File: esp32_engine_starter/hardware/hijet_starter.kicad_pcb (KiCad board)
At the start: 2 copper layers, 98 x 90 mm, 56 parts, among them J1 12V IN, J2 OUT, J3 IN, J4 I2C, J5 ESP32 VIN row, J6 ESP32 3V3 row, J7 OBD-II CAN, J8 GPS, Q1 2SC1815, U1 M78AR05-1, U2 PC817, U3 PC817, U4 PC817, U5 PC817, U6 PC817, U7 PC817, U8 PC817, U9 MCP2562-E/P

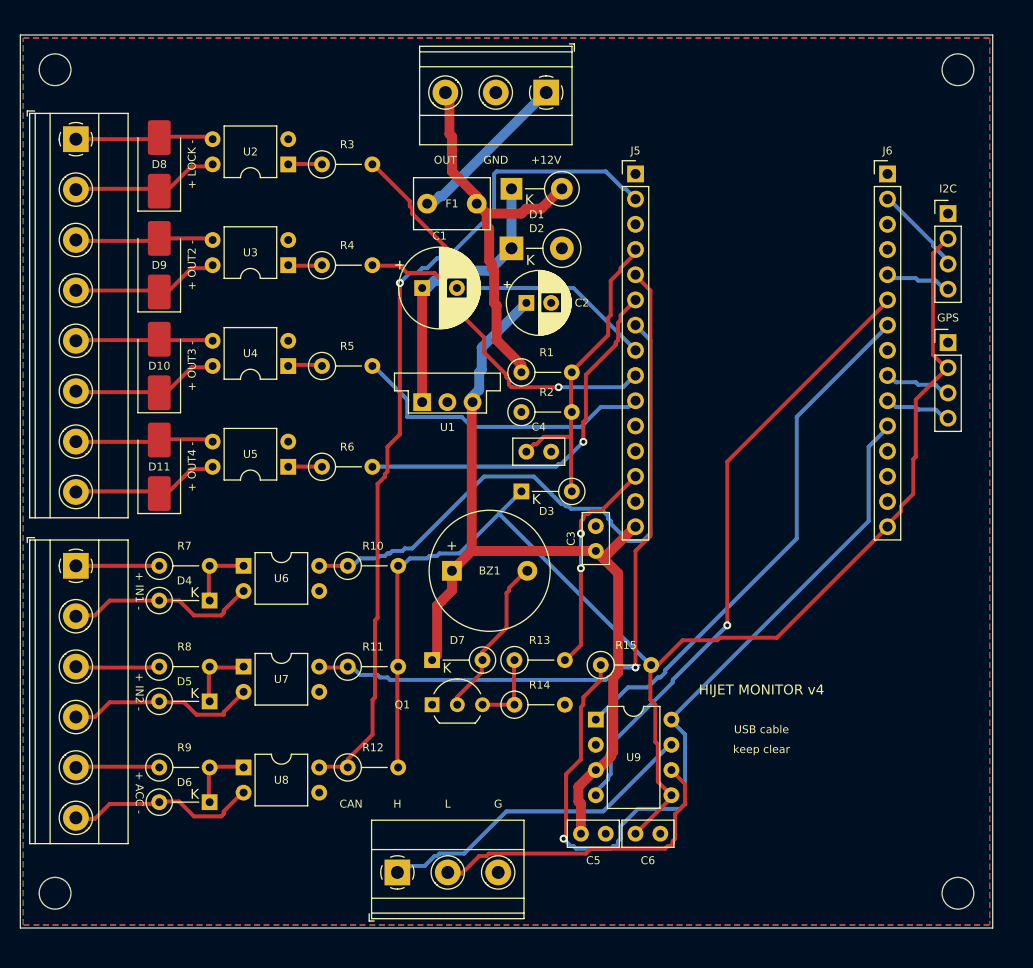
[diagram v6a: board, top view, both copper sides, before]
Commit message: ポリスイッチを RXEF110 に変更、逆接保護を SB340LS（3A）に変更
- RXEF090 が売り切れのため RXEF110（1.1A・72V）に変更
- RXEF の本体は幅 11〜13mm あり旧外形（7.5mm）では小さすぎたので、
  専用の外形（幅 12.8mm・穴 1.1mm）を作って基板上端に移動
- トリップまでの最大 2.2A に耐えるよう D1 を 1N5819（1A）から SB340LS（3A）へ
- 部品表・検証・文書を更新。全検証合格

Co-Authored-By: Claude Opus 5.5 <noreply@anthropic.com>
Claude-Session: https://claude.ai/code/session_011cXkDUypHbxixpJEznYmeT
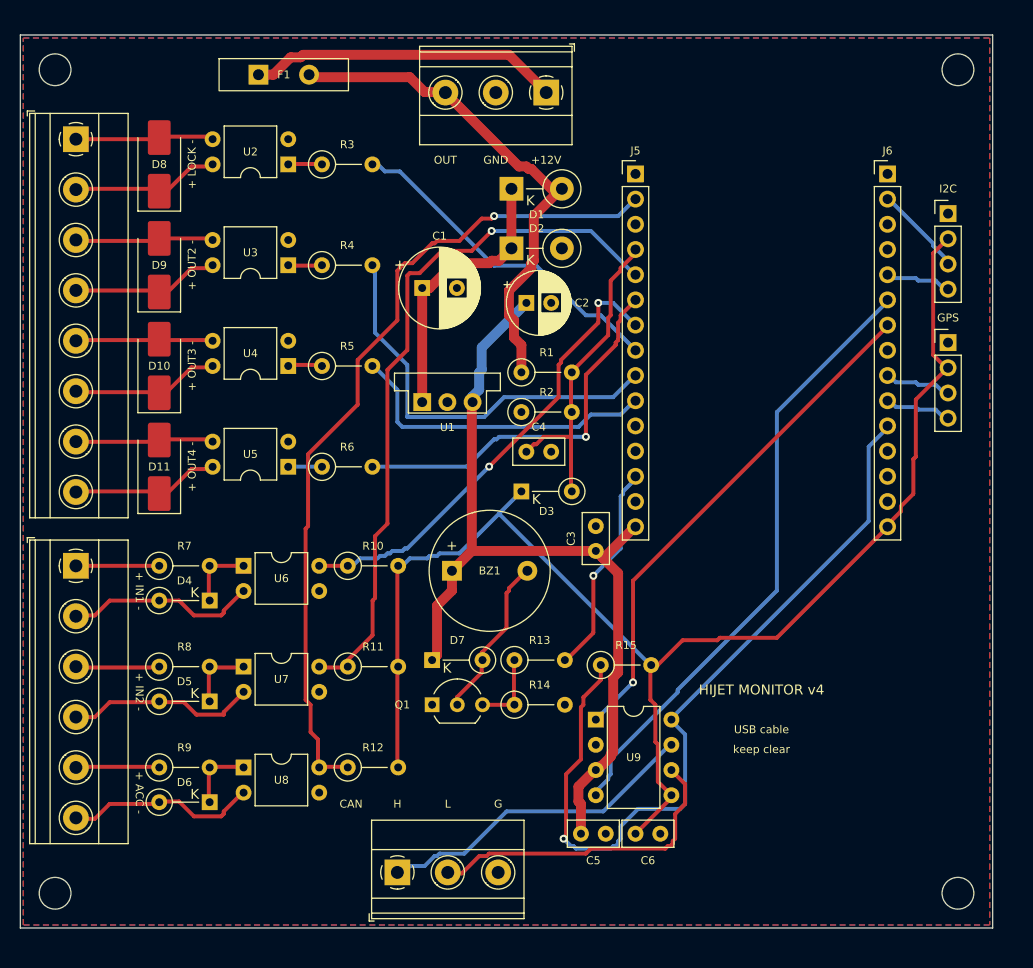
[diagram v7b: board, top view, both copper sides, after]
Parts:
- D1: value 1N5819 -> SB340LS; footprint D_DO-41_SOD81_P5.08mm_Vertical_KathodeUp -> D_DO-15_P5.08mm_Vertical_KathodeUp
- F1: value PTC 0.9A -> PTC 1.1A; footprint C_Disc_D7.5mm_W5.0mm_P5.00mm -> PTC_Radial_W12.8mm_T3.0mm_P5.10mm
- moved F1 21.4 mm to (24.0, 4.00)
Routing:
- net G33: track 62.1 -> 47.1 mm, vias 0 -> 2
- net BATT: track 16.7 -> 31.4 mm
- net 12V_F: track 40.0 -> 51.2 mm
- net G26: track 34.3 -> 41.5 mm, vias 1 -> 0
- net G35: track 73.8 -> 71.7 mm
- net G18: track 53.3 -> 52.0 mm, vias 0 -> 1
- net G25: track 35.4 -> 34.3 mm, vias 1 -> 0
- net G36: track 85.7 -> 84.5 mm
- net G27: track 31.3 -> 32.1 mm
- net G13: track 22.1 -> 21.4 mm, vias 2 -> 1
- net G19: vias 1 -> 0

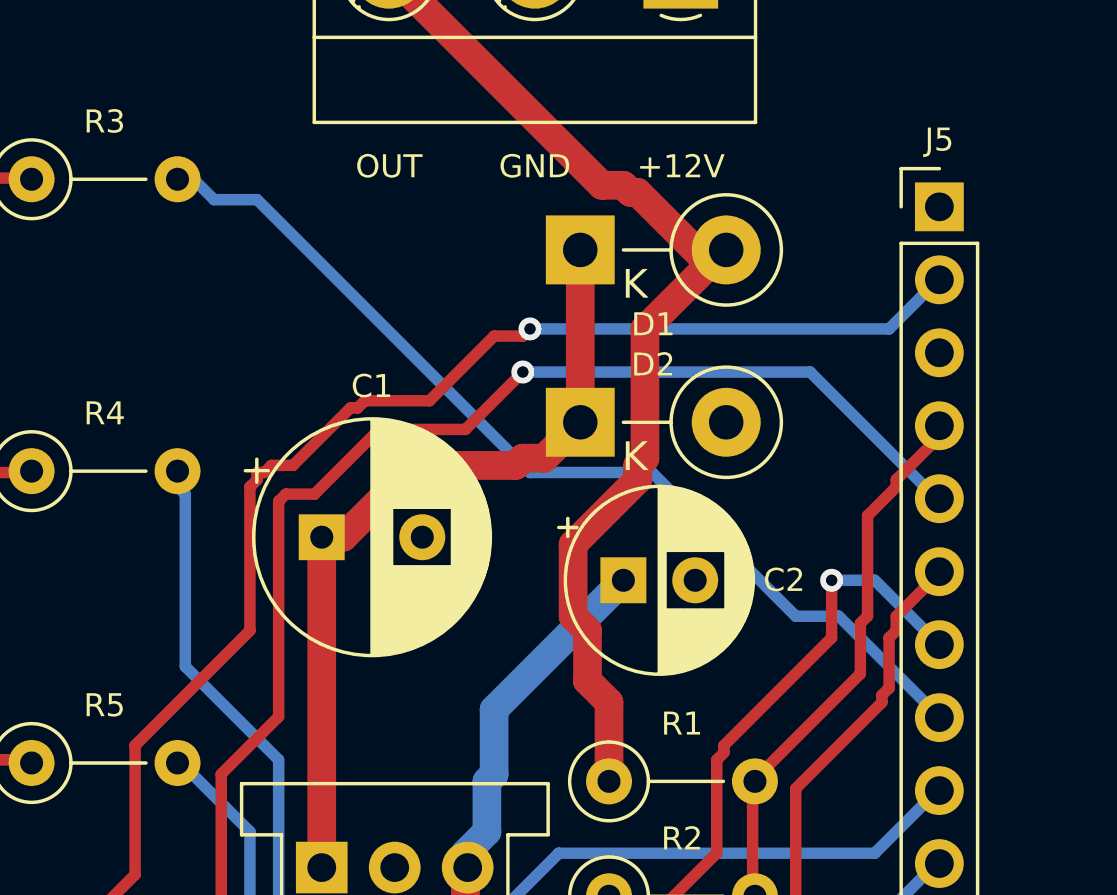
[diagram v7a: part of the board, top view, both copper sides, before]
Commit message: 電源の TVS を秋月で買える P4KE15A ＋ P4KE6.8CA の直列に変更
P6KE20A は秋月で扱いがないため。直列で導通しない上限 18.6V、
クランプ約 30V（18.9A 時）で M78AR05-1 の入力上限 32V 以内。
これで部品はすべて秋月でそろう。全検証合格。

Co-Authored-By: Claude Opus 5.5 <noreply@anthropic.com>
Claude-Session: https://claude.ai/code/session_011cXkDUypHbxixpJEznYmeT
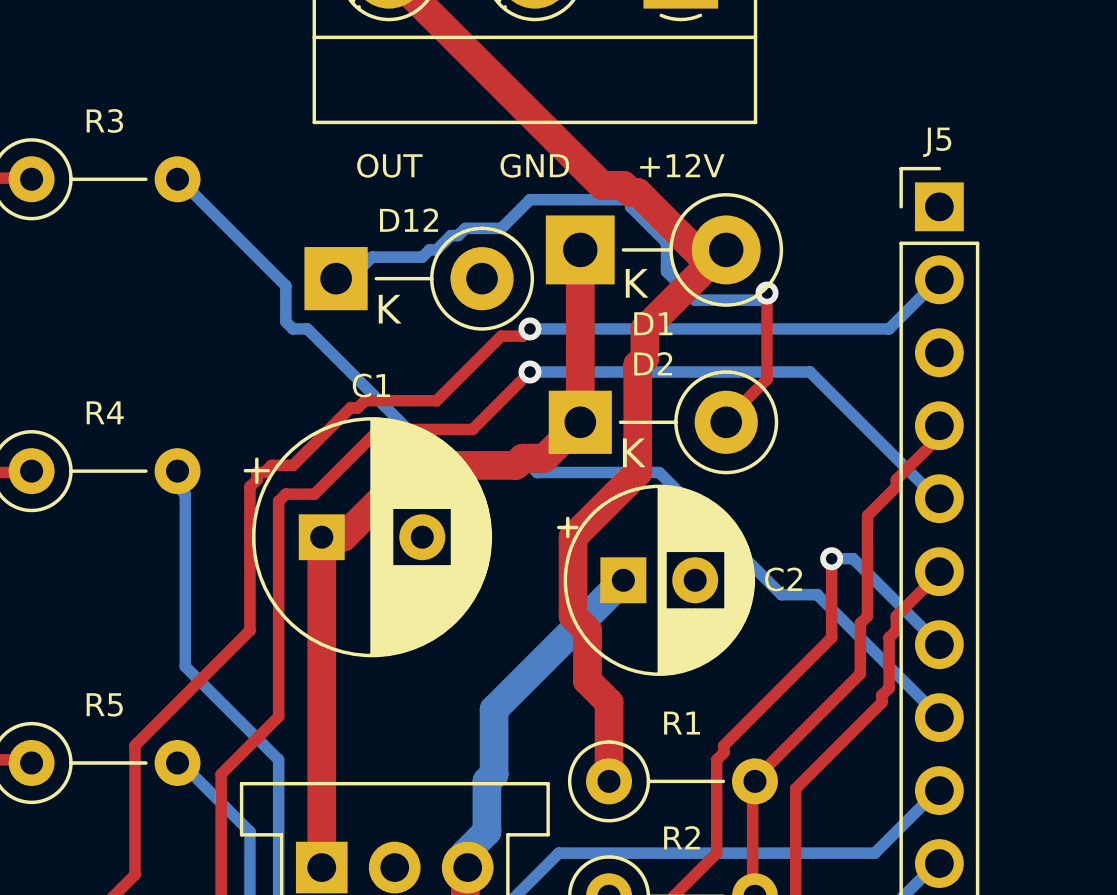
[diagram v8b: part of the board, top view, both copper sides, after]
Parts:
- added D12: P4KE6.8CA, D_DO-41_SOD81_P5.08mm_Vertical_KathodeUp, F.Cu at (41.0, 16.5)
- D2: value P6KE20A -> P4KE15A; footprint D_DO-15_P5.08mm_Vertical_KathodeUp -> D_DO-41_SOD81_P5.08mm_Vertical_KathodeUp
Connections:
- D2 pad 2: GND -> TVSM
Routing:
- net TVSM: track 0.00 -> 23.5 mm, vias 0 -> 1
- net G33: track 47.1 -> 48.2 mm
- net G25: track 34.3 -> 35.0 mm
